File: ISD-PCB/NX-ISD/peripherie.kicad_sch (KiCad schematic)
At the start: 16 parts, among them Q1 AO3400A, U7 TM-2025A

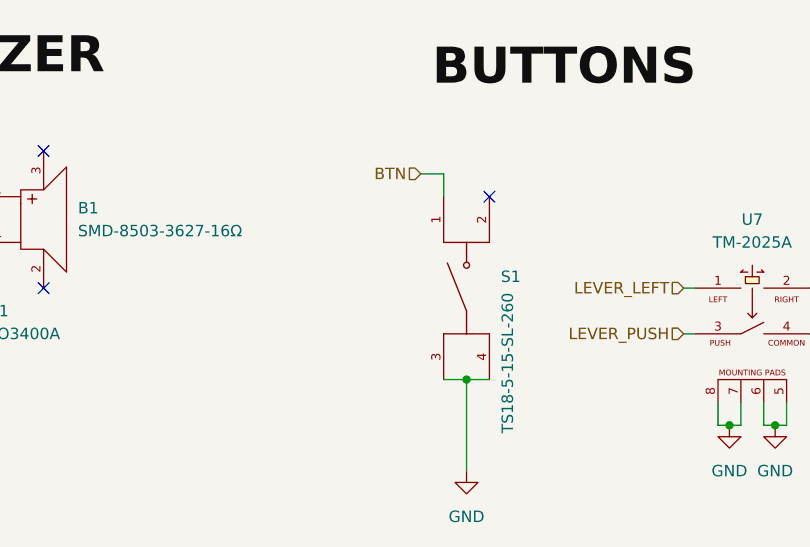
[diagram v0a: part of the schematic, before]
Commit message: Updated v1p0 files
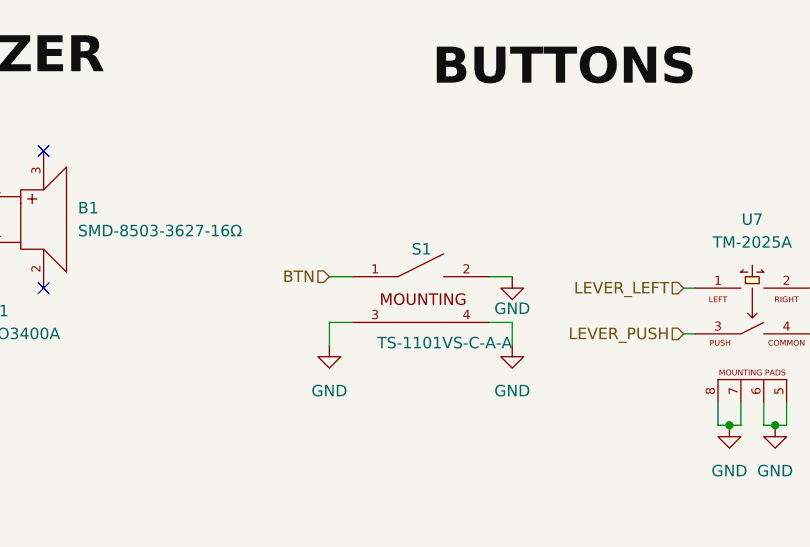
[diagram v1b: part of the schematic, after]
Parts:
- S1: value TS18-5-15-SL-260 -> TS-1101VS-C-A-A; Check_prices https://www.snapeda.com/parts/TS18-5-15-SL-260-SMT-TR/Same+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 -> (none); MANUFACTURER Same Sky -> (none); MF Same Sky -> XKB Connection; MP TS18-5-15-SL-260-SMT-TR -> (none); PARTREV 1.02 -> (none); STANDARD Manufacturer Recommendations -> (none); SnapEDA_Link https://www.snapeda.com/parts/TS18-5-15-SL-260-SMT-TR/Same+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 -> (none)
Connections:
- net GND: now also S1.2
- no-connect marks 4 -> 3

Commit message: v1p1 rework in progress
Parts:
- added G10, G11, G12, G13, G14, G15, G16: XL-1010RGBC-WS2812B, NX-AW-footprints:LED-SMD_4P-L1.0-W1.0-TL_XL-1010RGBC-WS2812B, symbol XL-1010RGBC-WS2812B:XL-1010RGBC-WS2812B
- added J1: 1-2328702-0, NX-AW-footprints:TE_1-2328702-0, symbol 1-2328702-0:1-2328702-0
- added Q4: AO3400A, Package_TO_SOT_SMD:SOT-23, symbol Transistor_FET:AO3400A
- added R10, R15: 220, Resistor_SMD:R_0402_1005Metric, symbol Device:R
- added R14: 10k, Resistor_SMD:R_0402_1005Metric, symbol Device:R
- added U14: ZDSD02GLGEAG, NX-AW-footprints:LGA-8_L8.0-W6.0-P1.27-TL_ZDSD02GLGEAG, symbol ZDSD02GLGEAG:ZDSD02GLGEAG
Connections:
- net +3V3: now also R15.1, U14.8 (VDD)
- net GND: now also G10.3 (GND), G11.3 (GND), G12.3 (GND), G13.3 (GND), G14.3 (GND), G15.3 (GND), G16.3 (GND), J1.1, J1.8, J1.S1 (SHIELD), J1.S2 (SHIELD), Q4.2 (S), R14.2, U14.4 (GND)
- net VN: now also G10.2 (VDD), G11.2 (VDD), G12.2 (VDD), G13.2 (VDD), G14.2 (VDD), G15.2 (VDD), G16.2 (VDD)
- net at G9.1 (DOUT): now also G10.4 (DIN)
- new net: Q4.1 (G), R10.1, R14.1
- new net: J1.10, Q4.3 (D)
- new net: G10.1 (DOUT), G11.4 (DIN)
- new net: G15.1 (DOUT), G16.4 (DIN)
- new net: J1.9, R15.2
- new net: G11.1 (DOUT), G12.4 (DIN)
- new net: G12.1 (DOUT), G13.4 (DIN)
- new net: G14.1 (DOUT), G15.4 (DIN)
- new net: G13.1 (DOUT), G14.4 (DIN)
- new net +2V8: J1.7
- new net CS_SD: U14.2 (DATA3)
- new net CS_TFT: J1.3
- new net DC: J1.2
- new net MISO: U14.6 (DAT0)
- new net MOSI: J1.5, U14.5 (CMD)
- new net PWM_TFT: R10.2
- new net RST: J1.6
- new net SCK: J1.4, U14.3 (CLK)
- no-connect marks 3 -> 5
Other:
- moved on the sheet: B1, D2, G1, G2, G3, G4, G5, G6, G7, G8, G9, Q1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

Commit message: finished v1p1 routing
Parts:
- D2: footprint Diode_SMD:D_0402_1005Metric -> Diode_SMD:D_SOD-523
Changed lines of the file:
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@@
 			)
 		)
-		(property "Footprint" "Diode_SMD:D_0402_1005Metric"
+		(property "Footprint" "Diode_SMD:D_SOD-523"
 			(at 169.545 43.18 0)
 			(hide yes)

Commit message: v1p3 major fix rework in progress
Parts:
- added C24, C25: 100n, Capacitor_SMD:C_0402_1005Metric, symbol Device:C
- added U16: TXB0106RGY, Package_DFN_QFN:Texas_RGY_R-PVQFN-N16_EP2.05x2.55mm, symbol Logic_LevelTranslator:TXB0106RGY
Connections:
- net +2V8: now also C25.1, U16.2 (V_{CCA}), U16.8 (OE)
- net +3V3: now also C24.1, U16.15 (V_{CCB})
- net CS_TFT: now also U16.14 (B2); no longer J1.3
- net DC: now also U16.16 (B1); no longer J1.2
- net GND: now also C24.2, C25.2, U16.10 (B6), U16.17 (GND), U16.7 (A6), U16.9 (GND)
- net MOSI: now also U16.11 (B5); no longer J1.5
- net RST: now also U16.13 (B3); no longer J1.6
- net SCK: now also U16.12 (B4); no longer J1.4
- new net LOW_CS_TFT: J1.3, U16.3 (A2)
- new net LOW_DC: J1.2, U16.1 (A1)
- new net LOW_MOSI: J1.5, U16.6 (A5)
- new net LOW_RST: J1.6, U16.4 (A3)
- new net LOW_SCK: J1.4, U16.5 (A4)
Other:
- note added: "(NPM DOES NOT REQUIRE DECOUPLING CAPACITORS DUE TO THE SHORT PATH OF ITS SUPPLY)"
- moved on the sheet: G1, G10, G11, G12, G13, G14, G15, G16, G2, G3, G4, G5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

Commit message: Added 3D-Renders to README
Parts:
- G10, G11, G12, G13, G14, G15, G16: footprint NX-AW-footprints:LED-SMD_4P-L1.0-W1.0-TL_XL-1010RGBC-WS2812B -> Global Footprints:LED-SMD_4P-L1.0-W1.0-TL_XL-1010RGBC-WS2812B
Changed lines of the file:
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@@
 			)
 		)
-		(property "Footprint" "NX-AW-footprints:LED-SMD_4P-L1.0-W1.0-TL_XL-1010RGBC-WS2812B"
+		(property "Footprint" "Global Footprints:LED-SMD_4P-L1.0-W1.0-TL_XL-1010RGBC-WS2812B"
 			(at 62.23 107.95 0)
 			(hide yes)
@@
 			)
 		)
-		(property "Footprint" "NX-AW-footprints:LED-SMD_4P-L1.0-W1.0-TL_XL-1010RGBC-WS2812B"
+		(property "Footprint" "Global Footprints:LED-SMD_4P-L1.0-W1.0-TL_XL-1010RGBC-WS2812B"
 			(at 115.57 129.54 0)
 			(hide yes)
@@
 			)
 		)
-		(property "Footprint" "NX-AW-footprints:LED-SMD_4P-L1.0-W1.0-TL_XL-1010RGBC-WS2812B"
+		(property "Footprint" "Global Footprints:LED-SMD_4P-L1.0-W1.0-TL_XL-1010RGBC-WS2812B"
 			(at 88.9 107.95 0)
 			(hide yes)
@@
 			)
 		)
-		(property "Footprint" "NX-AW-footprints:LED-SMD_4P-L1.0-W1.0-TL_XL-1010RGBC-WS2812B"
+		(property "Footprint" "Global Footprints:LED-SMD_4P-L1.0-W1.0-TL_XL-1010RGBC-WS2812B"
 			(at 115.57 107.95 0)
 			(hide yes)
@@
 			)
 		)
-		(property "Footprint" "NX-AW-footprints:LED-SMD_4P-L1.0-W1.0-TL_XL-1010RGBC-WS2812B"
+		(property "Footprint" "Global Footprints:LED-SMD_4P-L1.0-W1.0-TL_XL-1010RGBC-WS2812B"
 			(at 88.9 129.54 0)
 			(hide yes)
@@
 			)
 		)
-		(property "Footprint" "NX-AW-footprints:LED-SMD_4P-L1.0-W1.0-TL_XL-1010RGBC-WS2812B"
+		(property "Footprint" "Global Footprints:LED-SMD_4P-L1.0-W1.0-TL_XL-1010RGBC-WS2812B"
 			(at 35.56 129.54 0)
 			(hide yes)
@@
 			)
 		)
-		(property "Footprint" "NX-AW-footprints:LED-SMD_4P-L1.0-W1.0-TL_XL-1010RGBC-WS2812B"
+		(property "Footprint" "Global Footprints:LED-SMD_4P-L1.0-W1.0-TL_XL-1010RGBC-WS2812B"
 			(at 62.23 129.54 0)
 			(hide yes)

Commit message: v1p3 value hotfix - Display backlight resistor change
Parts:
- R15: value 220 -> 10
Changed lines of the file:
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@@
 			)
 		)
-		(property "Value" "220"
+		(property "Value" "10"
 			(at 204.47 121.92 90)
 			(show_name no)

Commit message: v1p3 - Isssues fixed
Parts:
- added C27: 100n, Capacitor_SMD:C_0402_1005Metric, symbol Device:C
- added R20, R21, R22: 51.1k, Resistor_SMD:R_0402_1005Metric, symbol Device:R
- renumbered C25 to C28, C24 to C29, D2 to D3, G7 to G10, G15 to G12, G4 to G13, G8 to G14, G12 to G15, G5 to G2, G9 to G3, G13 to G4, G2 to G5, G10 to G7, G14 to G8, G3 to G9, J1 to J2, Q1 to Q3, R5 to R23, R4 to R24, R10 to R25, R14 to R26, R15 to R27, U16 to U15, U7 to U16
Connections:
- net +3V3: now also C27.1, R20.1, R21.1, R22.1
- net CS_SD: now also R21.2
- net GND: now also C27.2
- net MISO: now also R22.2
- net MOSI: now also R20.2
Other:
- moved on the sheet: U14
